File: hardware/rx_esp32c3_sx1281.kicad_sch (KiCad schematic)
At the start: 47 parts, among them U1 ESP32-C3, U2 TLV75533PDQNR, U3 SX1281IMLTRT, X1 CJ17-400001010B20

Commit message: Root sheet: place the sub-sheets; ESC as the 4in1 top sheet
esc_4in1.kicad_sch is OpenESC-20x20's 4in1-mini top sheet (battery input,
shunt and INA186 current sense, 12V/3V3 regulators, four ESC channel
instances). Its channel sub-sheet keeps its original file name ESC.kicad_sch
so the top sheet is untouched. Root sheet: Power, IMU, OSD, Blackbox, Pads,
RP2354A, ESC, RX placed, no wiring.
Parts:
- removed TP1: RX, OpenRX-Shared:SolderPad_1.2x2.0mm, symbol Connector:TestPoint
- removed TP2: TX, OpenRX-Shared:SolderPad_1.2x2.0mm, symbol Connector:TestPoint
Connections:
- net ELRS_RX: now reaches U1.27 (U0RXD)
- net ELRS_TX: now reaches U1.28 (U0TXD)

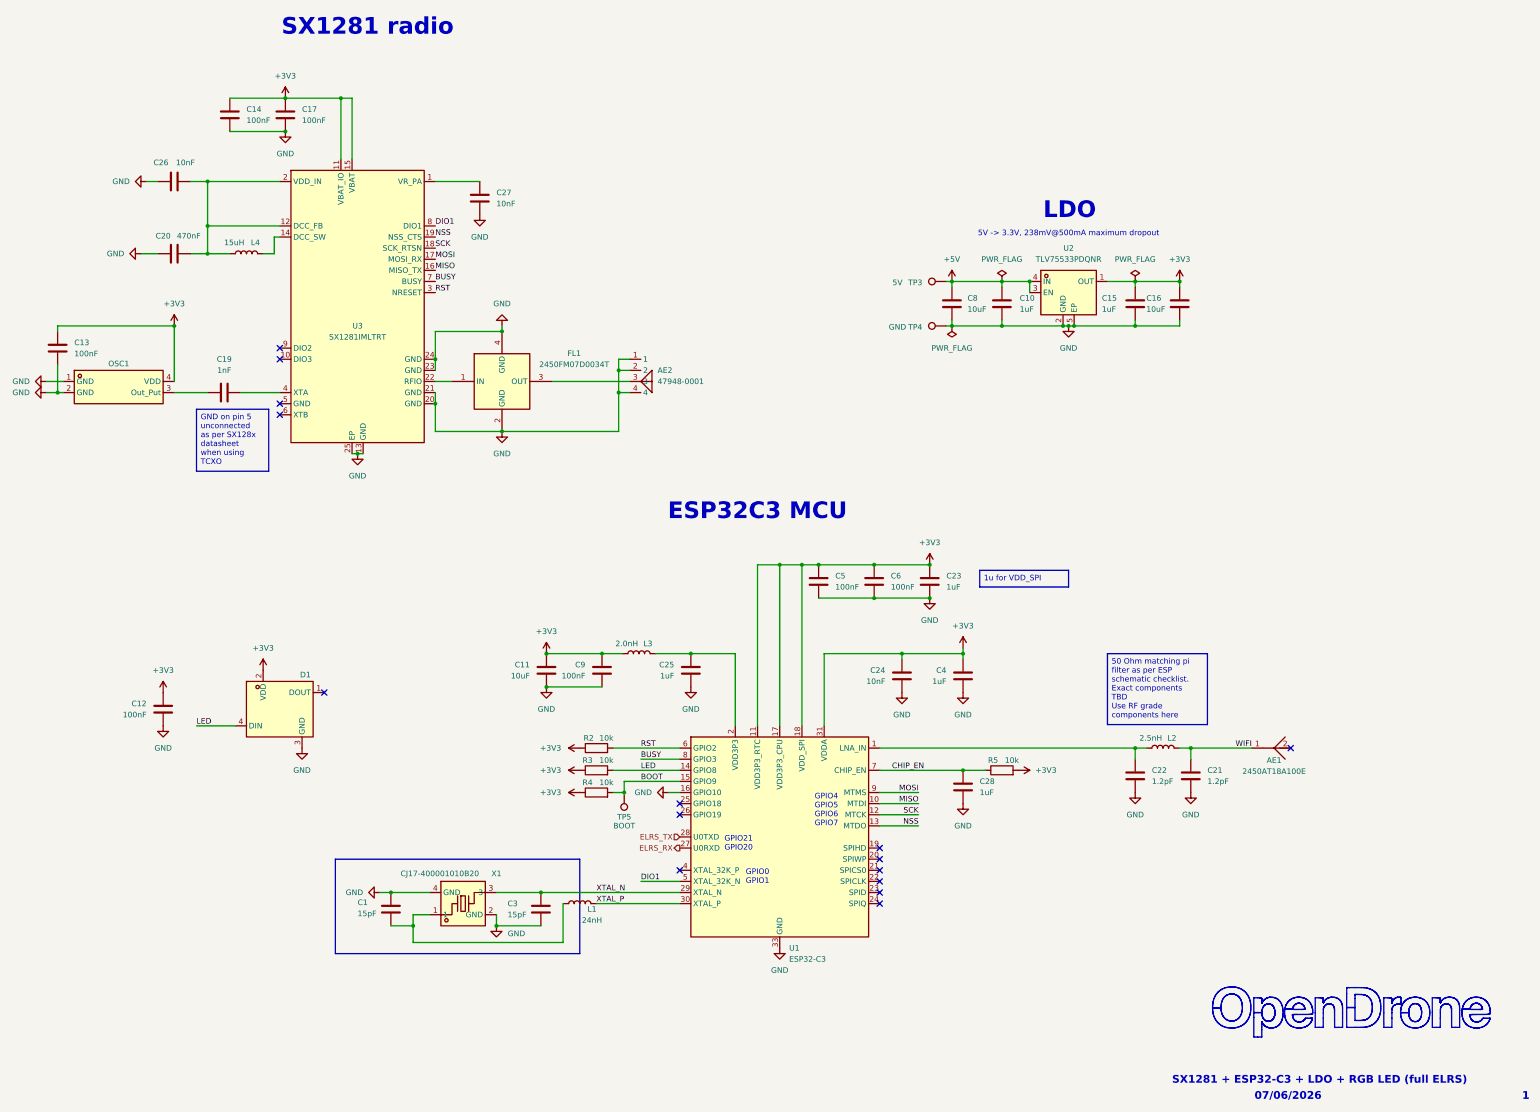
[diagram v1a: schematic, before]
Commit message: Net classes: VBAT, Phase, Power, Gate, USB, RF, Analog with colours and patterns
Replaces the stale 50Ohm /ELRS/* patterns inherited from the template.
Widths and clearances start from the line standard (0.09/0.09, via 0.35/0.20)
and the ESC boards' practice; USB and RF geometry still to be checked against
the chosen JLCPCB 6-layer stackup.
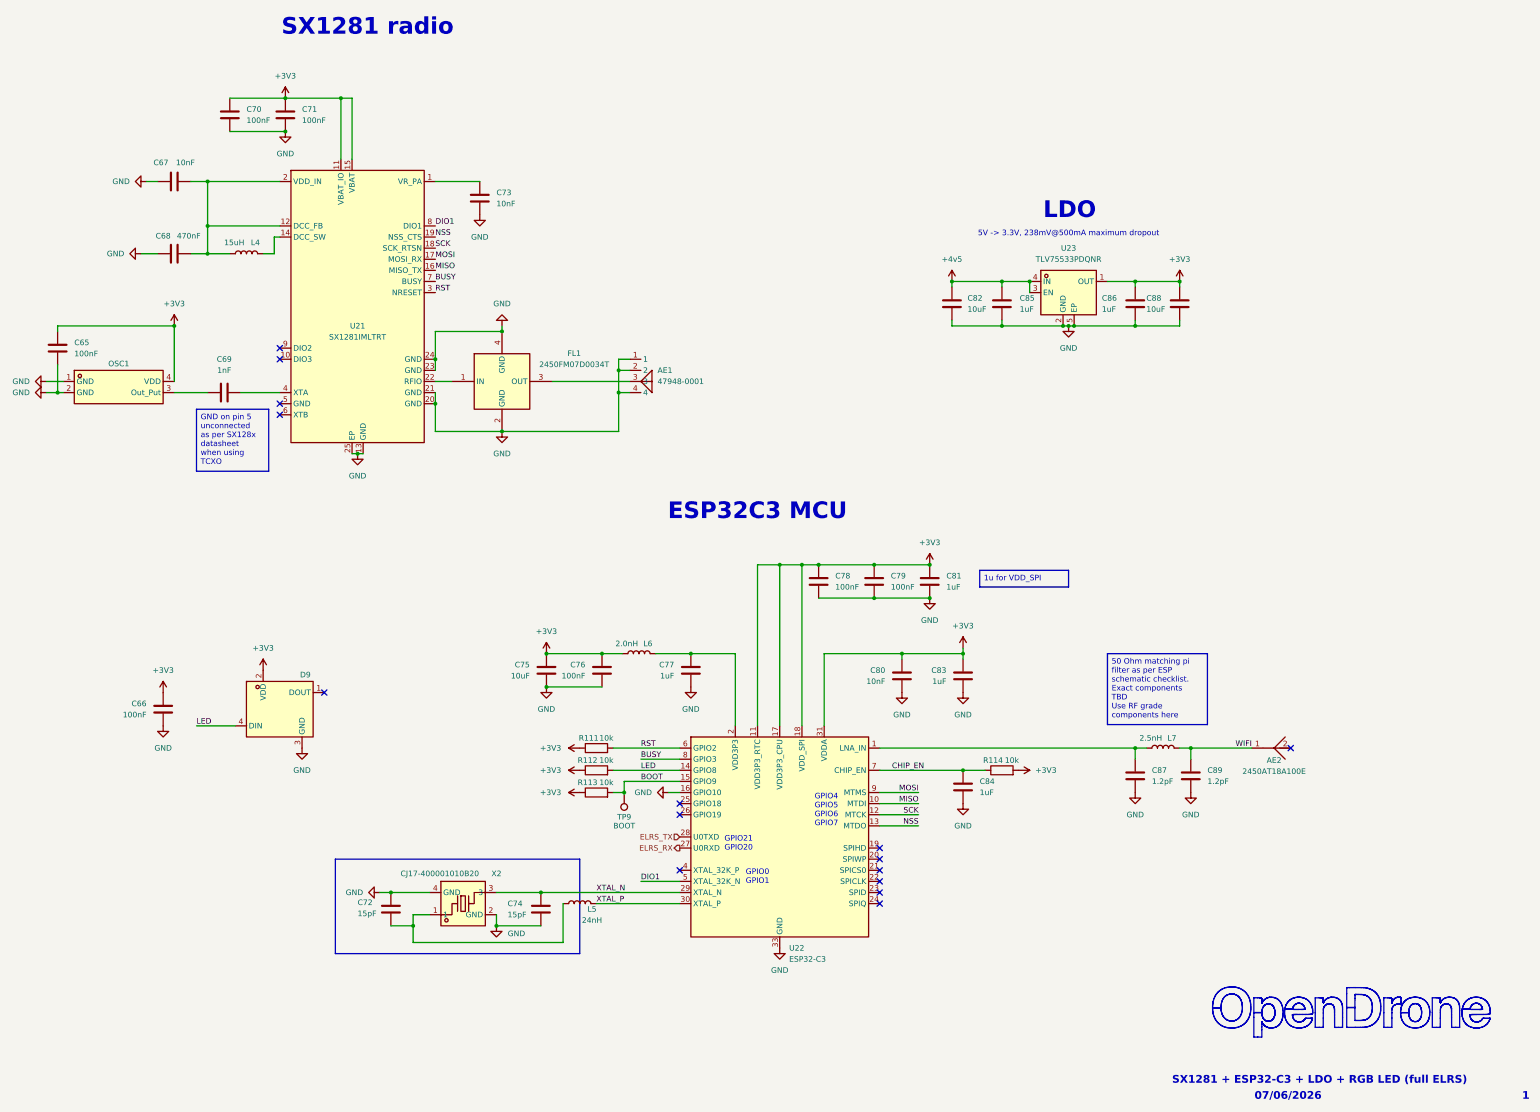
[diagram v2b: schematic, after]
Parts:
- removed TP3: 5V, OpenRX-Shared:SolderPad_1.2x2.0mm, symbol Connector:TestPoint
- removed TP4: GND, OpenRX-Shared:SolderPad_1.2x2.0mm, symbol Connector:TestPoint
- renumbered AE2 to AE1, AE1 to AE2, C13 to C65, C12 to C66, C26 to C67, C20 to C68, C19 to C69, C14 to C70, C17 to C71, C1 to C72, C27 to C73, C3 to C74, C11 to C75, C9 to C76, C25 to C77, C5 to C78, C6 to C79, C24 to C80, C23 to C81, C8 to C82, C4 to C83, C28 to C84, C10 to C85, C15 to C86, C22 to C87, C16 to C88, C21 to C89, D1 to D9, L1 to L5, L3 to L6, L2 to L7, R2 to R111, R3 to R112, R4 to R113, R5 to R114, TP5 to TP9, U3 to U21, U1 to U22, U2 to U23, X1 to X2
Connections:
- net +5V renamed +4v5
